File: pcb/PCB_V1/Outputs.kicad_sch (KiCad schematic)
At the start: 21 parts, among them J501 FAN1 / 3.5 mm, J511 FAN2 / 3.5 mm, J521 PUMP 24V / 6W, Q501 AO3400A, Q511 AO3400A, Q521 AO3422

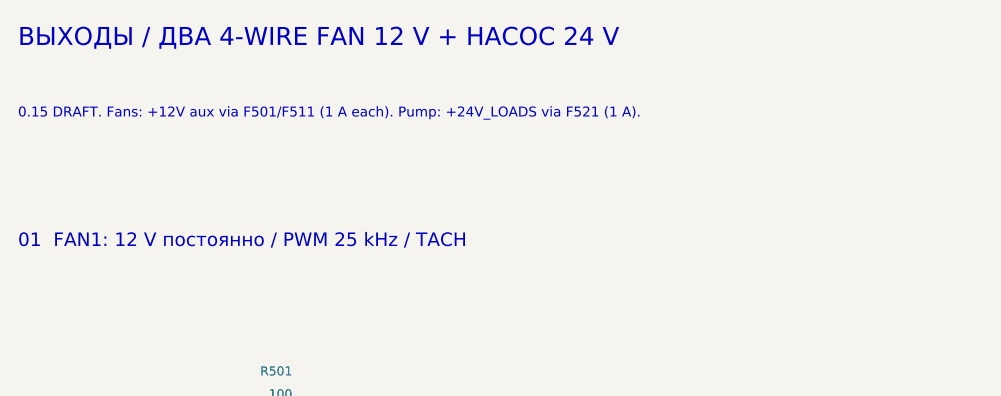
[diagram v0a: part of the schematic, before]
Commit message: pcb: revision 0.16 - drop redundant F903, restore CH1 inductor margin, clean DRC and docs
Schematic/board:
- remove F903 (7.5 A LED blade fuse): F711 6.3 A and F721 3 A already fuse
  each LED channel and F903 had the smallest margin; TP903/#FLG0603 removed,
  LED channel fuses and C710 now sit on +24V
- L711 back to Bourns SRP1770TA-470M with R715 0.027 ohm: CH1 OCP headroom
  3.17 A (was 0.34 A), worst-case winding loss 0.77 W (was 1.22 W)
- ESP32 footprint GrowBox:ESP32-WROOM-32E_NoVias without the 12 in-pad
  0.2 mm vias: DRC now 0 violations (only unrouted connections remain)
- 167 components; ERC 0/0

Checks and docs:
- new check_all.py runs ERC, netlist/board verification, sizing reports,
  BOM export and DRC; --write refreshes review/*_v16 and sheet images
- verify_netlist.py, verify_board.py, analyze_*.py updated for 0.16
- REDESIGN_24V.md -> DESIGN.md (current design only), new CHANGELOG.md,
  superseded 12 V documents in PCB_V1/history/, older reports in
  review/history/, README files rewritten as entry points
- cost estimation paused; v0.15 price audit kept as history

Co-Authored-By: Claude Opus 5.5 <noreply@anthropic.com>
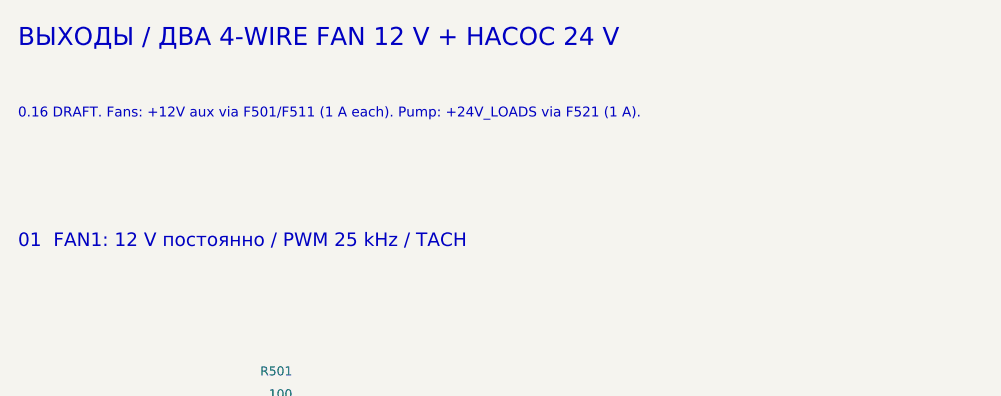
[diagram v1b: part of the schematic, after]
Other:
- note added: "0.16 DRAFT. Fans: +12V aux via F501/F511 (1 A each). Pump: +24V_LOADS via F521 (1 A)."
- note removed: "0.15 DRAFT. Fans: +12V aux via F501/F511 (1 A each). Pump: +24V_LOADS via F521 (1 A)."
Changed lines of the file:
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@@
 		(title "04 - Fans (12 V aux) and pump (24 V)")
 		(date "2026-09-27")
-		(rev "0.15-DRAFT")
+		(rev "0.16-DRAFT")
 		(company "GrowBox controller")
 		(comment 1 "Engineering draft; startup, thermal and fault qualification pending")
@@
 		)
 	)
-	(text "0.15 DRAFT. Fans: +12V aux via F501/F511 (1 A each). Pump: +24V_LOADS via F521 (1 A)."
+	(text "0.16 DRAFT. Fans: +12V aux via F501/F511 (1 A each). Pump: +24V_LOADS via F521 (1 A)."
 		(exclude_from_sim no)
 		(at 20.32 24.13 0)
